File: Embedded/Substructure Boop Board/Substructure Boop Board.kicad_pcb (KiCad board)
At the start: 2 copper layers, 30 x 30 mm, 36 parts, among them U1 PN5321A3HN_C1xx, U2 AD7142ACPZ-500RL7, U3 LD1117S33TR_SOT223, U5 R FFC, Y1 7M-27.120MAAJ-T

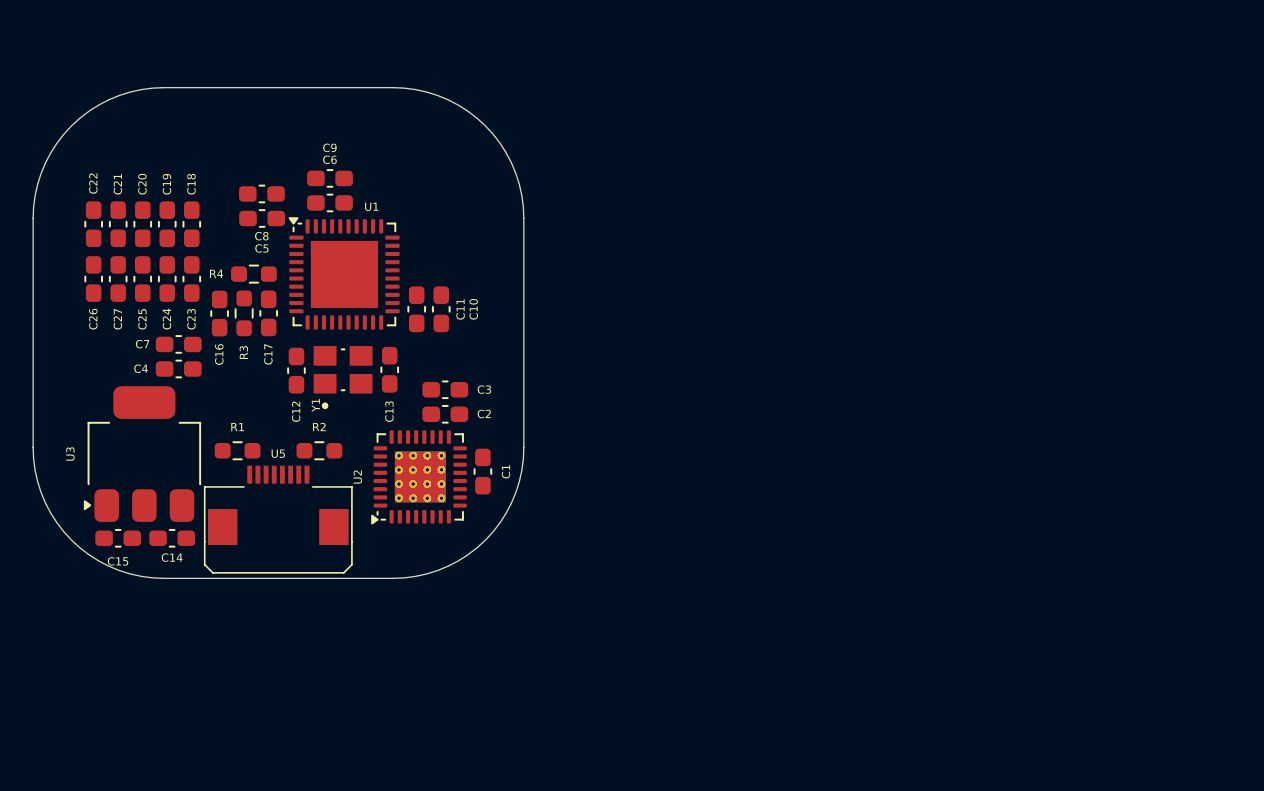
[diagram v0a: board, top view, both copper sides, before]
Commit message: Added PCB Antenna Design
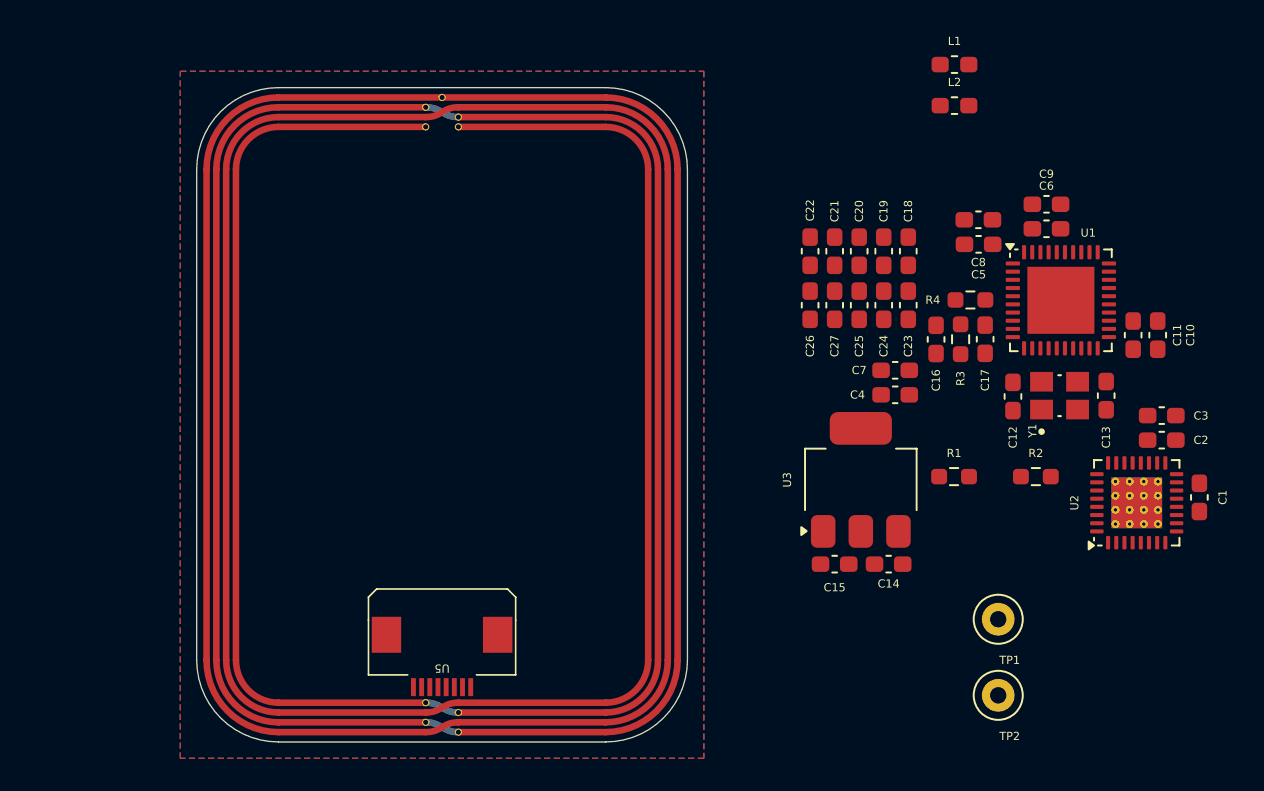
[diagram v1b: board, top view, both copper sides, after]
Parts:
- added L1: L, Inductor_SMD:L_0603_1608Metric_Pad1.05x0.95mm_HandSolder, F.Cu at (146.3, 48.6)
- added L2: L, Inductor_SMD:L_0603_1608Metric_Pad1.05x0.95mm_HandSolder, F.Cu at (146.3, 51.1)
- added TP1: TestPoint, TestPoint:TestPoint_Loop_D1.80mm_Drill1.0mm_Beaded, F.Cu at (149.0, 82.5)
- added TP2: TestPoint, TestPoint:TestPoint_Loop_D1.80mm_Drill1.0mm_Beaded, F.Cu at (149.0, 87.2)
- added U4: ~, PCB_Antenna:30 x 40 - 2 Pair 2 Layer 2 Turn Loop Antenna, F.Cu at (115.0, 70.0)
- moved C18 43.8 mm to (143.5, 60.0)
- moved C19 43.8 mm to (142.0, 60.0)
- moved C20 43.8 mm to (140.5, 60.0)
- moved C21 43.8 mm to (139.0, 60.0)
- moved C22 43.8 mm to (137.5, 60.0)
- moved C23 43.8 mm to (143.5, 63.3), turned to 90 degrees
- moved C24 43.8 mm to (142.0, 63.3), turned to 90 degrees
- moved C25 43.8 mm to (140.5, 63.3), turned to 90 degrees
- moved C26 43.8 mm to (137.5, 63.3), turned to -90 degrees
- moved C27 43.8 mm to (139.0, 63.3), turned to 90 degrees
- moved C1 43.8 mm to (161.3, 75.0)
- moved C12 43.8 mm to (149.9, 68.9)
- moved C14 43.8 mm to (142.3, 79.1)
- moved C5 43.8 mm to (147.8, 59.6)
- moved R1 43.8 mm to (146.3, 73.8)
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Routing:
- added copper zone on B.Cu, net GND
- added copper zone on F.Cu, net GND
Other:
- board size 30 x 30 mm -> 30 x 40 mm
- board text added: "LEFT RIGHT"

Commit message: Added Antenna LC tank values & EMC filter values
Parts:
- added R5: 1.5, Resistor_SMD:R_0603_1608Metric_Pad0.98x0.95mm_HandSolder, F.Cu at (134.5, 60.0)
- added R6: 1.5, Resistor_SMD:R_0603_1608Metric_Pad0.98x0.95mm_HandSolder, F.Cu at (134.5, 62.5)
- C18, C23: value NC -> 150pF
- C20, C25: value NC -> 22pF
- C22, C26: value NC -> 220pF
- L1, L2: value L -> 560nH
- R4: value 1.69K -> 1.7K
- U4: value ~ -> 0.35uH (Per Coil)
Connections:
- C18 pad 2: GND -> Net-(C18-Pad2)
- C19 pad 2: GND -> Net-(C19-Pad2)
- C23 pad 2: GND -> Net-(C18-Pad2)
- C24 pad 2: GND -> Net-(C19-Pad2)
- C26 pad 1: Net-(C25-Pad2) -> GND
- C26 pad 2: GND -> Net-(C25-Pad2)
- L1 pad 2: Net-(C18-Pad1) -> Net-(C20-Pad2)
- L2 pad 2: Net-(C23-Pad1) -> Net-(C25-Pad2)
- R4 pad 2: Net-(C23-Pad1) -> Net-(C25-Pad2)
- U4 pad 1: Net-(C18-Pad1) -> Net-(R5-Pad2)
- U4 pad 2: Net-(C23-Pad1) -> Net-(R6-Pad2)

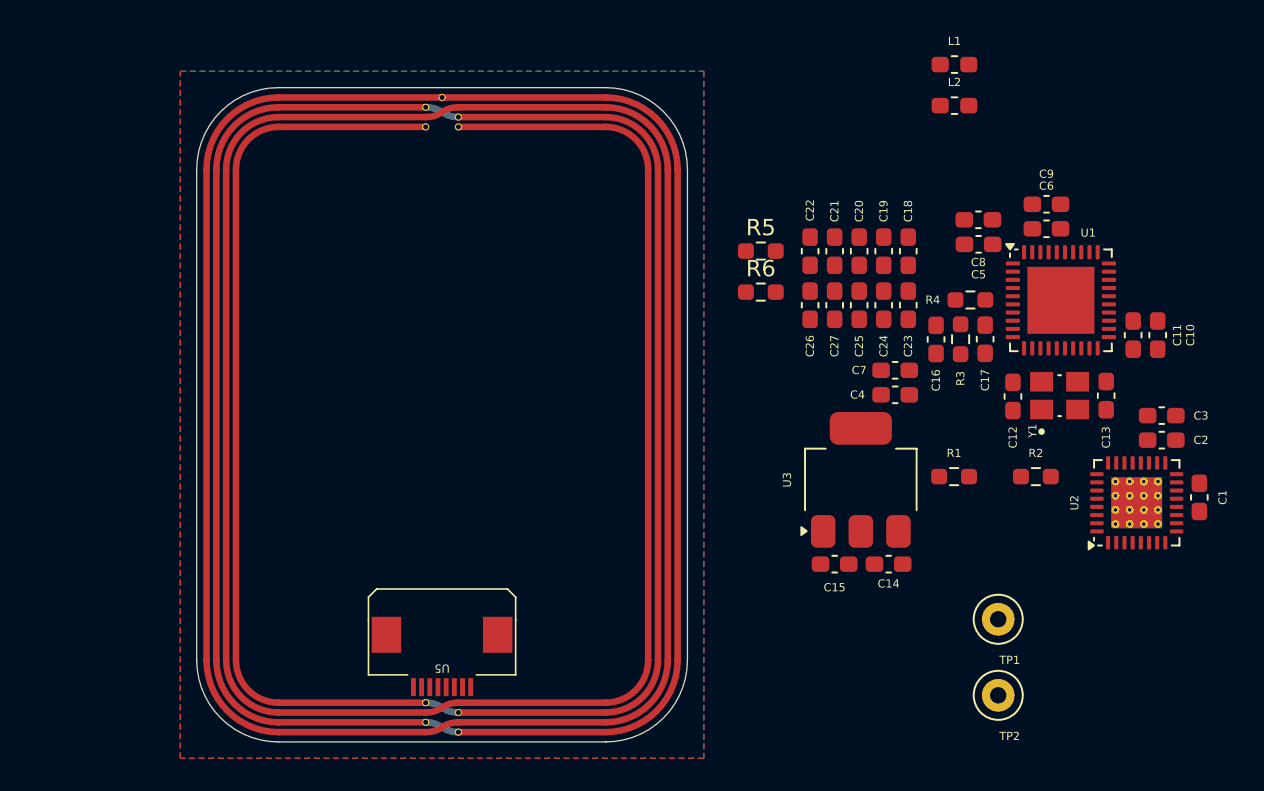
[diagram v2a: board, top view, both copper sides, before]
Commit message: Modified Antenna component placement positions
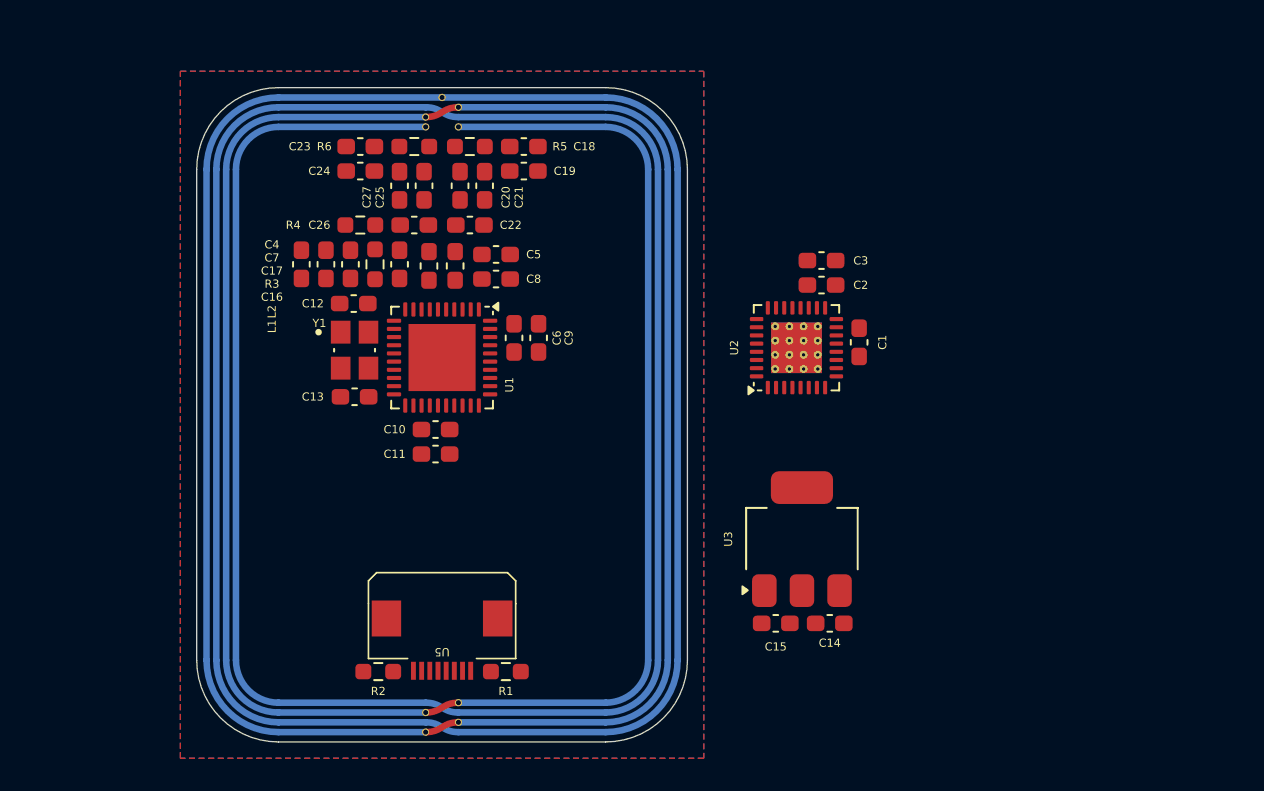
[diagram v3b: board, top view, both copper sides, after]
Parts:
- removed TP1, TP2: TestPoint, TestPoint:TestPoint_Loop_D1.80mm_Drill1.0mm_Beaded
- U4: moved to B.Cu
- moved C13 46.0 mm to (109.7, 68.9), turned to 180 degrees
- moved C10 44.5 mm to (114.6, 70.9), turned to 0 degrees
- moved C11 43.3 mm to (114.6, 72.4), turned to 0 degrees
- moved Y1 43.2 mm to (109.7, 66.0), turned to 0 degrees
- moved R2 41.9 mm to (111.1, 85.7), turned to 180 degrees
- moved C12 40.7 mm to (109.6, 63.2), turned to 0 degrees
- moved C17 39.1 mm to (109.4, 60.8)
- moved U1 38.0 mm to (115.0, 66.5), turned to -90 degrees
- moved R4 37.6 mm to (110.0, 58.4), turned to 0 degrees
- moved C4 37.2 mm to (106.4, 60.8), turned to 90 degrees
- moved R3 36.1 mm to (110.9, 60.8)
- moved C7 35.4 mm to (107.9, 60.8), turned to 90 degrees
- moved C23 34.9 mm to (110.0, 53.6), turned to 180 degrees
- moved L2 33.6 mm to (114.2, 60.9), turned to 90 degrees
- moved C6 33.2 mm to (119.4, 65.3), turned to -90 degrees
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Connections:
- C18 pad 2: Net-(C18-Pad2) -> GND
- C19 pad 2: Net-(C19-Pad2) -> GND
- C23 pad 2: Net-(C18-Pad2) -> GND
- C24 pad 2: Net-(C19-Pad2) -> GND

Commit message: Added Capacitive sensor component placement
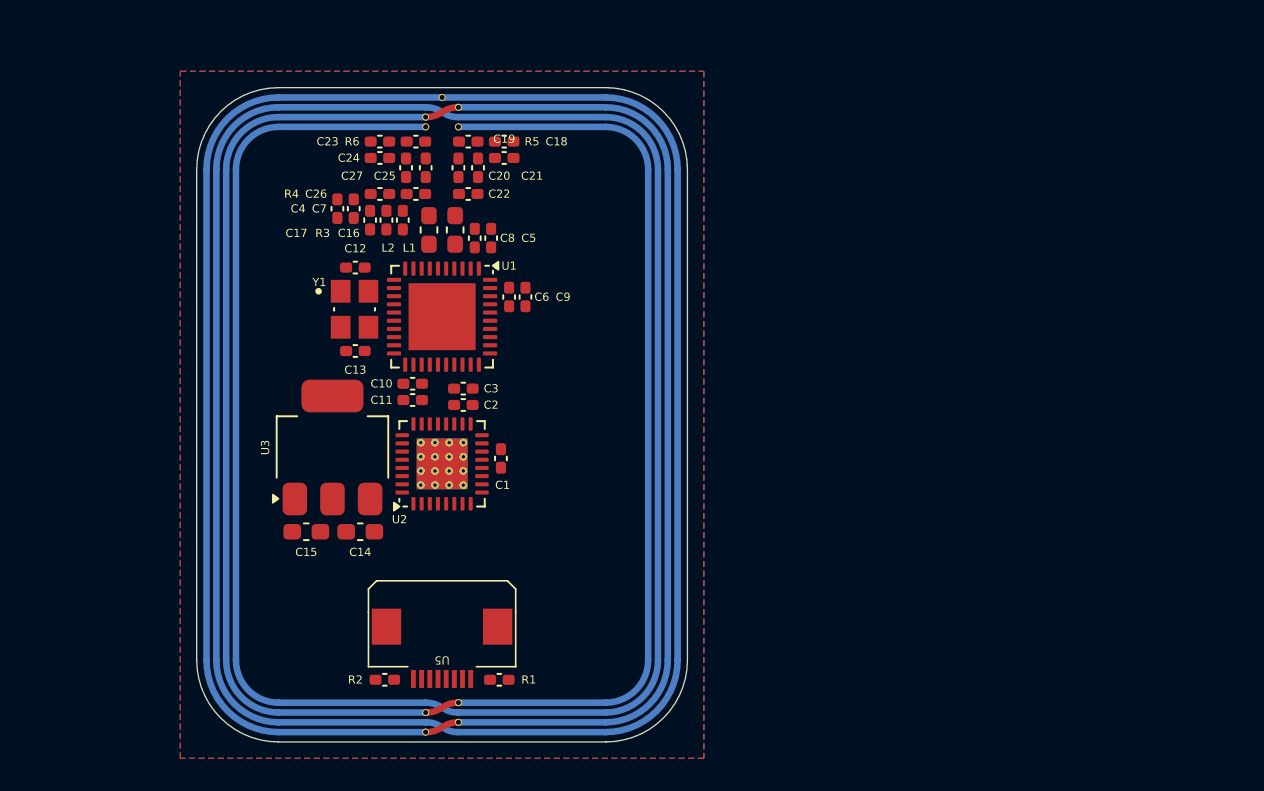
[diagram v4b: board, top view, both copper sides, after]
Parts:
- C1, C10, C11, C12, C13, C16, C17, C18, C19, C2, C20, C21, C22, C23, C24, C25, C26, C27, C3, C4, C5, C6, C7, C8, C9: footprint Capacitor_SMD:C_0603_1608Metric_Pad1.08x0.95mm_HandSolder -> Capacitor_SMD:C_0402_1005Metric_Pad0.74x0.62mm_HandSolder
- R1, R2, R3, R4, R5, R6: footprint Resistor_SMD:R_0603_1608Metric_Pad0.98x0.95mm_HandSolder -> Capacitor_SMD:C_0402_1005Metric_Pad0.74x0.62mm_HandSolder
- moved C15 29.2 mm to (106.7, 77.2)
- moved U3 29.2 mm to (108.3, 72.0)
- moved C14 29.2 mm to (110.0, 77.2)
- moved C3 23.3 mm to (116.3, 68.4)
- moved C2 23.1 mm to (116.3, 69.4)
- moved C1 23.0 mm to (118.6, 72.7)
- moved U2 22.8 mm to (115.0, 73.0)
- moved C4 4.05 mm to (108.6, 57.4)
- moved C7 3.80 mm to (109.6, 57.4)
- moved C11 3.58 mm to (113.2, 69.1), turned to 180 degrees
- moved C10 3.13 mm to (113.2, 68.1), turned to 180 degrees
- moved C17 2.95 mm to (110.6, 58.1)
- moved C8 2.82 mm to (117.0, 59.2), turned to -90 degrees
- moved C13 2.80 mm to (109.7, 66.1)
- moved R3 2.79 mm to (111.6, 58.1)
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
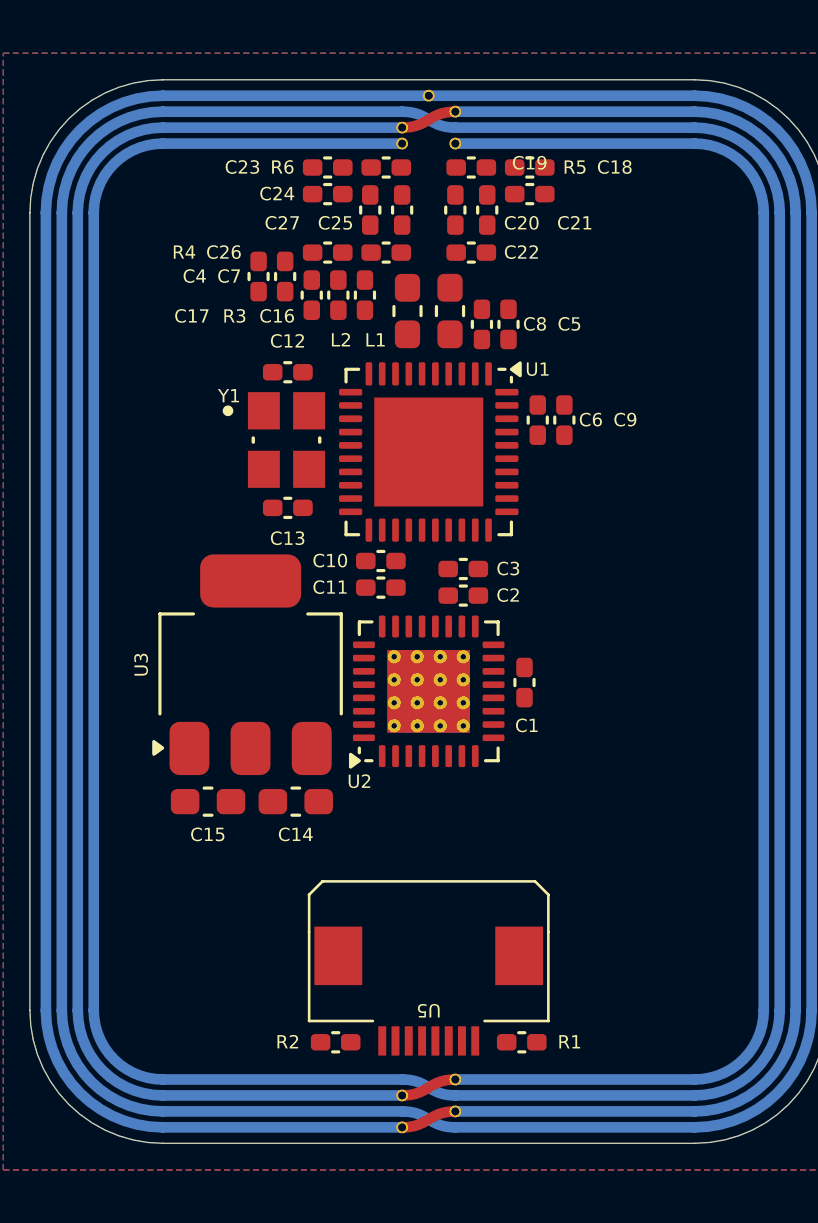
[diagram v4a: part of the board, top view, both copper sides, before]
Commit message: Added Routing
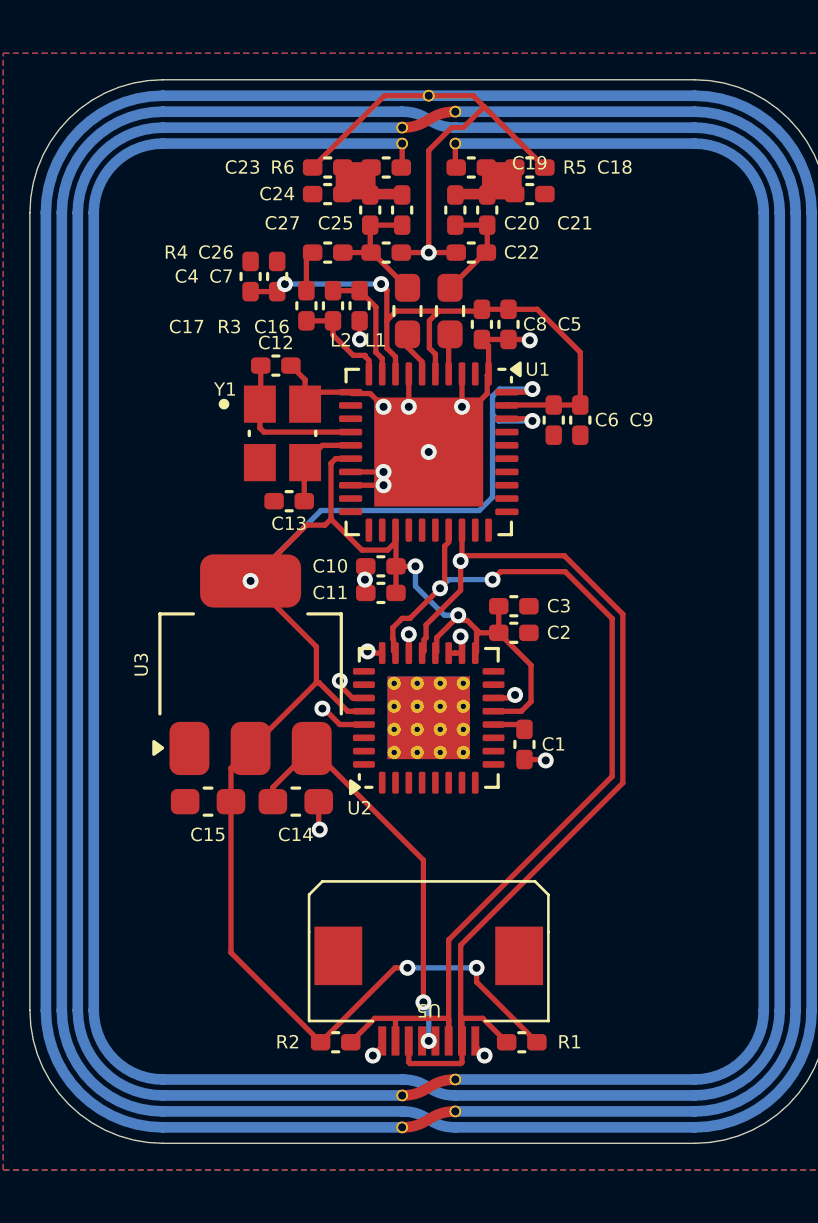
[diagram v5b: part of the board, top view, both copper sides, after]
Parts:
- moved C2 2.36 mm to (118.2, 70.8), turned to 0 degrees
- moved C3 2.36 mm to (118.2, 69.8), turned to 0 degrees
- moved C1 2.33 mm to (118.6, 75.0), turned to 90 degrees
- moved U2 1.00 mm to (115.0, 74.0)
- moved C6 0.60 mm to (119.7, 62.8)
- moved C9 0.60 mm to (120.7, 62.8)
- moved C12 0.51 mm to (109.2, 60.8)
- moved C16 0.45 mm to (112.4, 58.5)
- moved C17 0.45 mm to (110.4, 58.5)
- moved R3 0.45 mm to (111.4, 58.5)
- moved C4 0.30 mm to (108.3, 57.4)
- moved C7 0.30 mm to (109.3, 57.4)
- moved Y1 0.29 mm to (109.5, 63.3)
- moved C13 0.25 mm to (109.8, 65.8)
- moved C10 0.20 mm to (113.2, 68.3)
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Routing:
- net +3V3: track 0.00 -> 80.0 mm, vias 0 -> 7
- net GND: track 0.00 -> 58.3 mm, vias 0 -> 20
- net I2C SDA: track 0.00 -> 37.5 mm, vias 0 -> 1
- net I2C SCL: track 0.00 -> 37.3 mm, vias 0 -> 2
- net Net-(U1-AVDD): track 0.00 -> 24.1 mm, vias 0 -> 2
- net +5V: track 0.00 -> 15.9 mm, vias 0 -> 2
- net Net-(U1-OSCIN): track 0.00 -> 5.69 mm
- net Net-(C25-Pad2): track 0.00 -> 5.23 mm
- net Net-(U1-VMID): track 0.00 -> 4.48 mm
- net Net-(C20-Pad2): track 0.00 -> 4.16 mm
- net Net-(U1-RX): track 0.00 -> 3.82 mm
- net Net-(U1-OSCOUT): track 0.00 -> 3.45 mm
- net Net-(U1-TX2): track 0.00 -> 1.72 mm
- net Net-(C17-Pad2): track 0.00 -> 1.53 mm
- net Net-(U1-TX1): track 0.00 -> 1.51 mm
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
